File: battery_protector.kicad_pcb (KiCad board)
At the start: 4 copper layers, 93.7 x 93.8 mm, 104 parts, among them J1 TB005-762-02BE, J2 TB005-762-02BE, J3 USB_C_Receptacle_USB2.0_16P, J5 Conn_01x12, Q1 SQJQ184ER, Q2 SQJQ184ER, Q3 SQJQ184ER, Q4 SQJQ184ER, Q5 MMBT3904, Q6 MMBT3904, SW1 SW_DPDT_x2, SW2 PTS647SN50SMTR2_LFS, SW3 PTS647SN50SMTR2_LFS, U1 LMR38020SDDAR, U2 AP2112K-3.3, U3 TPS2116DRL, U4 CP2102N-Axx-xQFN28, U5 ESP32-C3-WROOM-02, U6 LIS3DH, U7 2ED4820EMXUMA2

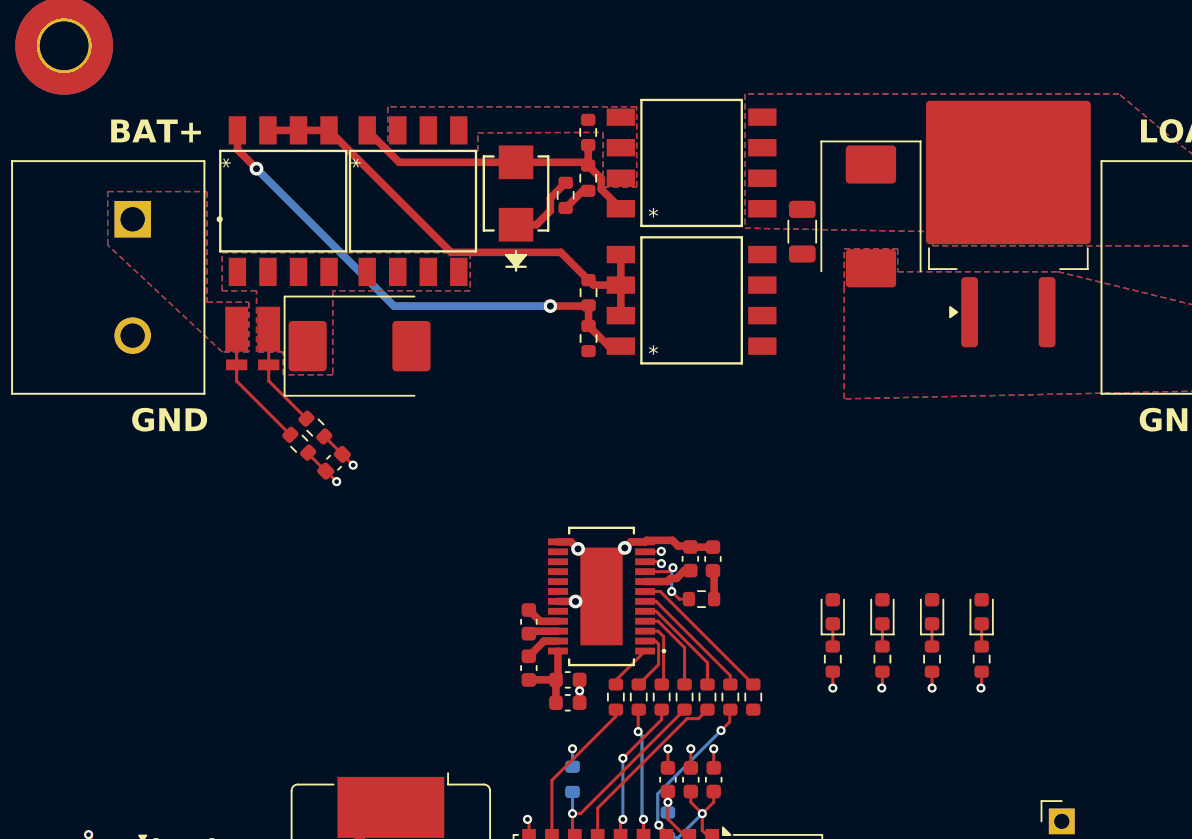
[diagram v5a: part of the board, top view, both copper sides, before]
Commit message: Routed Gate Driver, will have to move all components to top layer for simplicity and move the switching reg farther away from the mcu
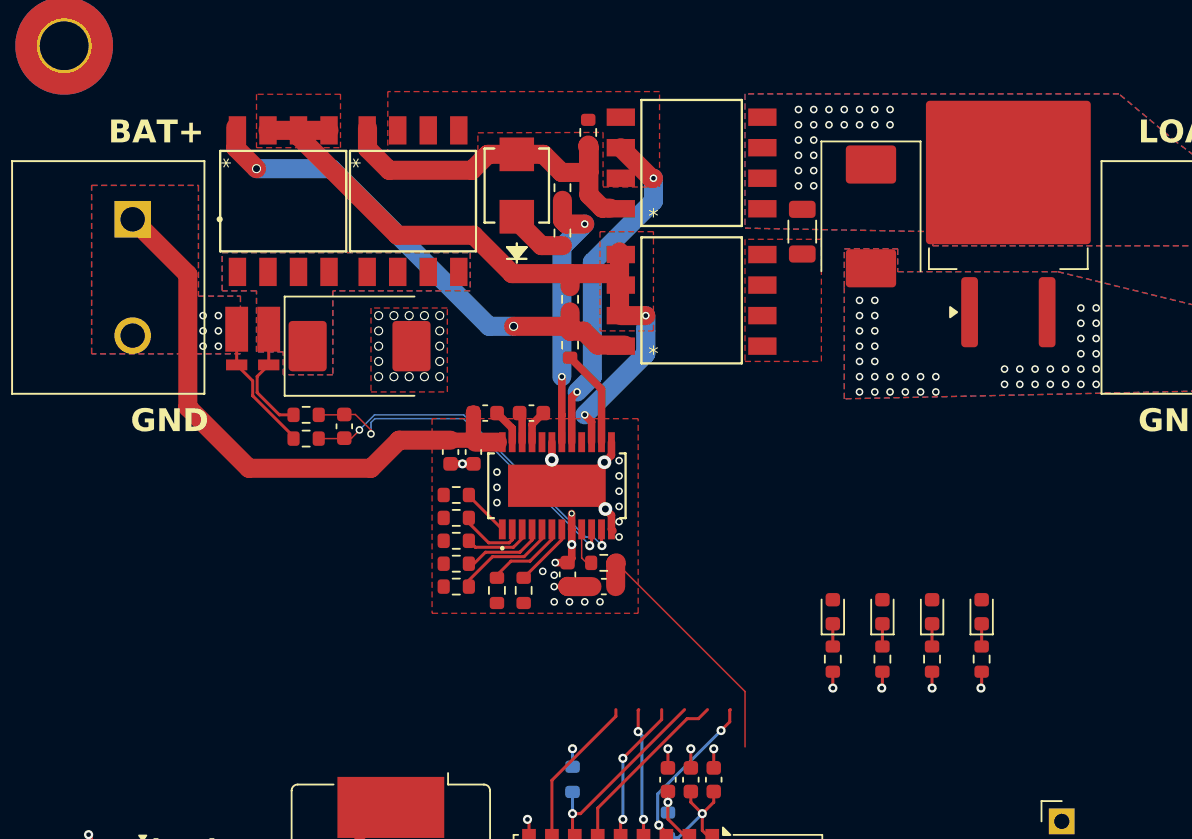
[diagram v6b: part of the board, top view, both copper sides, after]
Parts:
- moved C21 18.1 mm to (106.7, 88.9), turned to -90 degrees
- moved R41 18.0 mm to (107.1, 97.8), turned to 0 degrees
- moved R40 17.3 mm to (107.1, 96.2), turned to 0 degrees
- moved C19 16.9 mm to (109.0, 86.4), turned to 180 degrees
- moved R39 16.9 mm to (107.1, 94.8), turned to 0 degrees
- moved R37 16.9 mm to (107.1, 91.8), turned to 0 degrees
- moved R42 16.8 mm to (109.8, 98.0)
- moved R38 16.8 mm to (107.1, 93.2), turned to 0 degrees
- moved R43 16.6 mm to (111.5, 98.0)
- moved C18 16.2 mm to (108.2, 88.9), turned to -90 degrees
- moved C20 13.7 mm to (112.0, 86.4), turned to 180 degrees
- moved C24 8.11 mm to (114.4, 97.0), turned to -90 degrees
- moved U7 7.82 mm to (113.7, 91.1), turned to 90 degrees
- moved C17 7.38 mm to (116.8, 97.8), turned to 180 degrees
- moved R36 6.83 mm to (116.7, 96.2)
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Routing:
- net BAT+: track 13.6 -> 47.1 mm, vias 0 -> 6
- net /GateDriver/SOURCE_A: track 0.00 -> 22.5 mm, vias 0 -> 2
- net /GateDriver/IS_N: track 3.79 -> 23.9 mm
- net /GateDriver/IS_P: track 3.77 -> 23.8 mm
- net /GateDriver/GATE_A: track 1.94 -> 17.7 mm, vias 0 -> 2
- net /MCU/GD_IS: track 1.89 -> 17.1 mm
- net /GateDriver/SOURCE_B: track 31.3 -> 45.5 mm, vias 0 -> 2
- net /GateDriver/GATE_B: track 0.00 -> 6.39 mm
- net Net-(U7-ENABLE): track 9.61 -> 4.21 mm
- net Net-(D6-A): track 20.5 -> 24.2 mm
- net GND: track 82.0 -> 79.1 mm, vias 58 -> 132
- net Net-(U7-MISO): track 8.18 -> 5.40 mm
- net Net-(U7-CSO): track 4.87 -> 2.41 mm, vias 2 -> 0
- net Net-(D6-K): track 4.87 -> 3.63 mm
- net Net-(Q1-G): track 32.5 -> 33.4 mm
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- added copper zone on F.Cu, net /GateDriver/SOURCE_B
- added copper zone on F.Cu, net Net-(Q3-D)
- removed copper zone on B.Cu, net /GateDriver/SOURCE_A

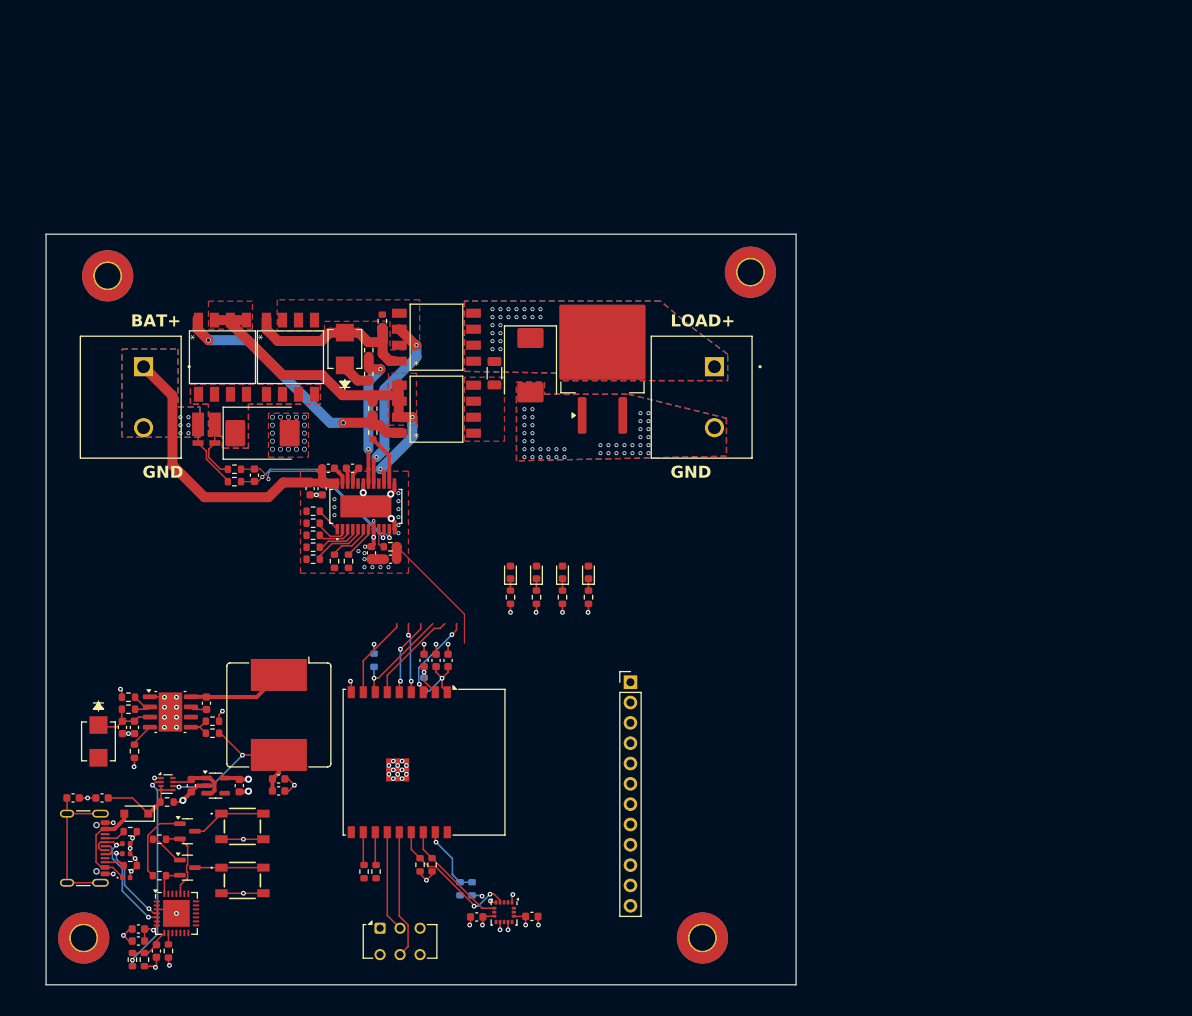
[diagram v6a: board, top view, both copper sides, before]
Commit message: More routing, changed the footprints of some caps.
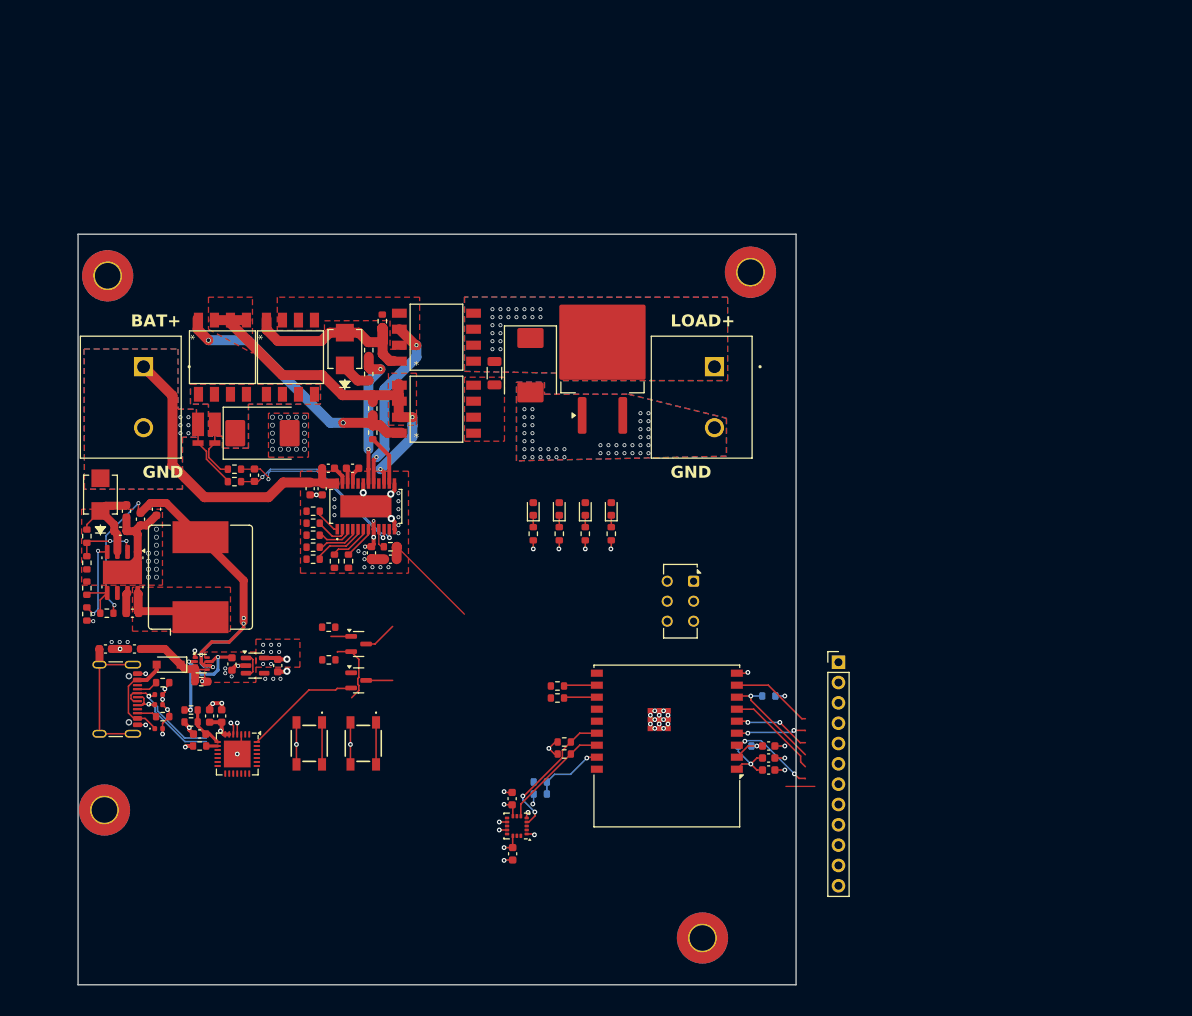
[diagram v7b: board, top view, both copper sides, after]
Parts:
- moved SW1 58.5 mm to (154.6, 100.5), turned to -90 degrees
- moved R25 49.6 mm to (164.1, 114.8), turned to 180 degrees
- moved C14 44.4 mm to (164.0, 121.1), turned to 0 degrees
- moved C12 43.3 mm to (164.0, 122.6), turned to 0 degrees
- moved C13 42.4 mm to (164.0, 124.1), turned to 0 degrees
- moved R27 40.8 mm to (161.1, 121.1), turned to 0 degrees
- moved C8 38.1 mm to (85.5, 92.8), turned to -90 degrees
- moved C7 37.0 mm to (87.5, 91.5), turned to -90 degrees
- moved R30 34.3 mm to (109.0, 110.3)
- moved R31 33.9 mm to (109.0, 106.3)
- moved R33 33.5 mm to (137.6, 113.6), turned to 0 degrees
- moved U5 33.1 mm to (150.8, 118.3), turned to 180 degrees
- moved R23 32.0 mm to (91.8, 116.6), turned to 0 degrees
- moved Q5 31.7 mm to (112.8, 108.4)
- moved Q6 31.7 mm to (112.8, 112.9)
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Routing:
- net +5V0_board: track 23.9 -> 61.0 mm, vias 2 -> 6
- net Net-(SW1B-B): track 16.2 -> 0.00 mm
- net Net-(SW1A-B): track 12.7 -> 0.00 mm
- net +5V0: track 33.2 -> 20.6 mm, vias 2 -> 3
- net /MCU/DTR: track 3.95 -> 14.4 mm
- net Net-(U1-RT): track 2.97 -> 10.5 mm, vias 0 -> 2
- net Net-(Q5-B): track 9.90 -> 2.52 mm
- net GND: track 79.1 -> 83.4 mm, vias 132 -> 142
- net Net-(Q6-B): track 4.14 -> 0.00 mm
- net Net-(D10-K): track 8.56 -> 12.6 mm
- net /DC-DC/5V_BUCK_EN: track 4.34 -> 8.16 mm, vias 0 -> 2
- net Net-(U1-SW): track 12.1 -> 14.5 mm
- net Net-(U1-FB): track 4.36 -> 5.54 mm
- net /MCU/RTS: track 9.51 -> 8.40 mm
- net /DC-DC/USB_DP: track 14.5 -> 15.4 mm
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- added copper zone on F.Cu, net +3V3
- added copper zone on F.Cu, net +5V0
- added copper zone on F.Cu, net Net-(U1-SW)
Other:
- board size 93.7 x 93.8 mm -> 89.7 x 93.8 mm

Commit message: Finished Routing and ran DRC. Will need final review of schematics and layout with Austin. Will also need to update BOM.
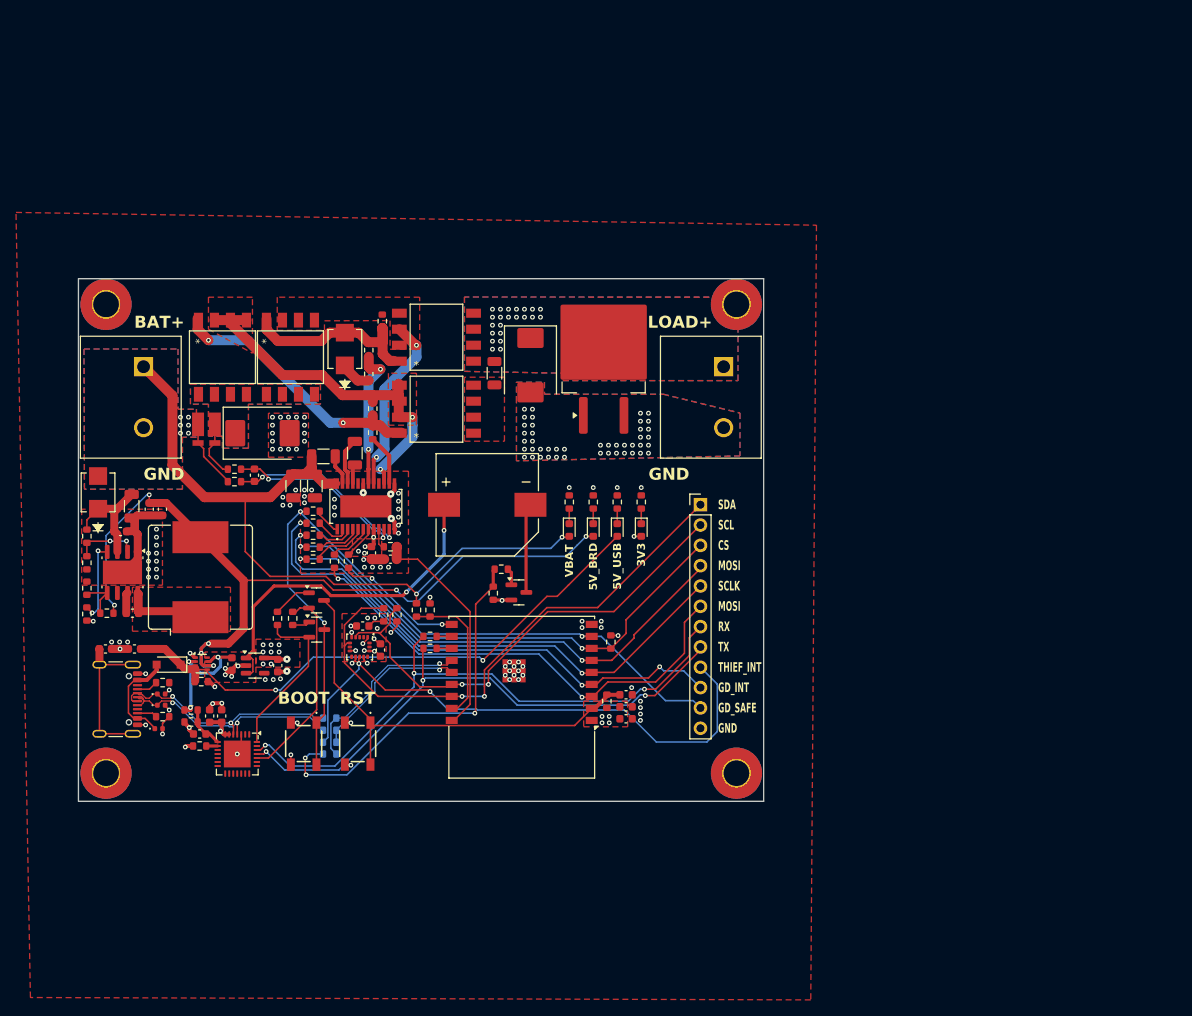
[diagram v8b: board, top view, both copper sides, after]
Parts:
- removed SW1: SW_DPDT_x2, Button_Switch_THT:SW_CK_JS202011CQN_DPDT_Straight
- added BZ1: Buzzer, custom_footprints:MagneticBuzzer_CT_1205C_SMT_TR, F.Cu at (128.7, 91.1)
- added Q7: MMBT3904, Package_TO_SOT_SMD:SOT-23, F.Cu at (132.8, 101.9)
- added R44: 0, Resistor_SMD:R_0603_1608Metric, B.Cu at (109.2, 117.6)
- added R45: 0, Resistor_SMD:R_0603_1608Metric, B.Cu at (109.2, 120.6)
- added R46: 0, Resistor_SMD:R_0603_1608Metric, B.Cu at (109.2, 119.1)
- added R47: 1k, Resistor_SMD:R_0603_1608Metric, F.Cu at (130.6, 99.0)
- added R48: 75k, Resistor_SMD:R_0603_1608Metric, F.Cu at (129.6, 102.0)
- added R9: 0, Resistor_SMD:R_0603_1608Metric, B.Cu at (109.2, 122.1)
- C1: value 150nF X7R -> 150n
- C10, C24, C9: value 1uF -> 1u
- C15: value 10uF -> 10u
- C16: value 100nF -> 100n
- C17: value 10nF -> 10n
- C18, C20: value 220nF -> 220n; footprint Capacitor_SMD:C_0603_1608Metric -> Capacitor_SMD:C_1206_3216Metric
- C19: value 2.2uF -> 2.2u; footprint Capacitor_SMD:C_0603_1608Metric -> Capacitor_SMD:C_1206_3216Metric
- C21: value 4.7uF -> 4.7u; footprint Capacitor_SMD:C_0603_1608Metric -> Capacitor_SMD:C_1206_3216Metric
- C22: value 4.7uF -> 4.7u
- C23: value 0.1uF -> 0.1u
- C3: footprint Capacitor_SMD:C_0603_1608Metric -> Capacitor_SMD:C_1206_3216Metric
- R25, R27, R34, R35: moved to F.Cu
- moved C16 30.4 mm to (115.5, 109.1), turned to 90 degrees
- moved U6 29.8 mm to (112.9, 108.7), turned to -90 degrees
- moved C15 28.5 mm to (113.3, 106.1), turned to 180 degrees
- moved R29 28.5 mm to (115.9, 104.7), turned to 90 degrees
- moved R35 26.8 mm to (121.7, 104.1), turned to -90 degrees
- moved R34 26.5 mm to (120.0, 104.1), turned to 90 degrees
- moved R28 26.3 mm to (117.6, 104.7), turned to 90 degrees
- moved J5 26.2 mm to (155.5, 90.9)
- moved H8 21.0 mm to (160.0, 124.5)
- moved R25 20.9 mm to (144.3, 108.1), turned to -90 degrees
- moved U5 19.1 mm to (132.7, 112.2)
- moved C12 18.9 mm to (146.2, 116.2)
- moved C13 18.9 mm to (146.2, 117.7)
- moved C14 18.9 mm to (146.2, 114.7)
- moved R27 18.1 mm to (143.8, 115.5), turned to 90 degrees
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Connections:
- J5 pad 3: /MISO -> /~{CS}
- J5 pad 4: /SCLK -> /MOSI
- J5 pad 5: /MOSI -> /SCLK
- J5 pad 6: /~{CS} -> /MISO
- J5 pad 7: /MCU/TXD -> /MCU/RXD
- J5 pad 8: /MCU/RXD -> /MCU/TXD
- U5 pad 13: Net-(SW1A-B) -> /MCU/DN
- U5 pad 14: Net-(SW1B-B) -> /MCU/DP
- U6 pad 11: unconnected-(U6-INT1-Pad11) -> /MCU/THIEF_INT
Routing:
- net /MCU/~{GD_SAFE}: track 18.9 -> 96.9 mm, vias 0 -> 3
- net /MCU/RXD: track 0.00 -> 74.3 mm, vias 0 -> 3
- net /MCU/THIEF_INT: track 0.00 -> 70.9 mm, vias 0 -> 2
- net /MCU/TXD: track 0.00 -> 70.5 mm, vias 0 -> 3
- net +5V0_USB: track 11.5 -> 72.3 mm, vias 0 -> 2
- net /MCU/GD_INT: track 8.73 -> 65.7 mm, vias 2 -> 3
- net /SCLK: track 9.68 -> 65.2 mm
- net /MCU/I2C1_SDA: track 14.1 -> 69.4 mm, vias 0 -> 2
- net BAT+: track 47.1 -> 102.3 mm, vias 6 -> 8
- net /MOSI: track 12.0 -> 61.4 mm, vias 0 -> 2
- net /~{CS}: track 13.4 -> 62.6 mm, vias 1 -> 2
- net /MISO: track 10.8 -> 59.9 mm
- net /MCU/BEEP_BEEP_BITCH: track 0.00 -> 47.9 mm, vias 0 -> 3
- net /MCU/I2C1_SCL: track 17.5 -> 60.7 mm
- net +5V0_board: track 61.0 -> 103.3 mm, vias 6 -> 7
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- added copper zone on In2.Cu, net GND
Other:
- board size 89.7 x 93.8 mm -> 85.7 x 65.3 mm
- board text added: "3V3"
- board text added: "5V_BRD"
- board text added: "5V_USB"
- board text added: "BEEP_EN"
- board text added: "BOOT"
- board text added: "CS"
- board text added: "GD_INT"
- board text added: "GD_SAFE"
- board text added: "LOAD CURRENT PATH"
- board text added: "MOSI"
- board text added: "RST"
- board text added: "RX"
- board text added: "SCL"
- board text added: "SCLK"
- board text added: "SDA"
- board text added: "THIEF_INT"
- board text added: "TX"
- board text added: "USB_DN"
- board text added: "USB_DP"
- board text added: "VBAT"
